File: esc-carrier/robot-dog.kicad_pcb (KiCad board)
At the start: 2 copper layers, 74.3 x 78.1 mm, 35 parts, among them J1 Conn_01x02, J10 Conn_01x02, J11 Conn_01x04, J12 Conn_01x04, J13 Conn_01x04, J2 Conn_01x04, J3 Conn_01x04, J4 Conn_01x03, J5 Conn_01x05, J6 Conn_01x05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

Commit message: Final version for manufacture
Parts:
- added REF**: MountingHole_3.2mm_M3_Pad, MountingHole:MountingHole_3.2mm_M3_Pad, F.Cu at (196.5, 94.2)
- added REF**: MountingHole_3.2mm_M3_Pad, MountingHole:MountingHole_3.2mm_M3_Pad, F.Cu at (210.7, 40.9)
- added REF**: MountingHole_3.2mm_M3_Pad, MountingHole:MountingHole_3.2mm_M3_Pad, F.Cu at (146.1, 40.9)
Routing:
- net Net-(J11-Pad1): track 137.1 -> 139.0 mm
- net Net-(J11-Pad2): track 128.5 -> 129.2 mm
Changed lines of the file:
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@@
       (outputformat 1)
       (mirror false)
-      (drillshape 1)
+      (drillshape 0)
       (scaleselection 1)
-      (outputdirectory "")
+      (outputdirectory "out")
     )
   )
@@
     )
   )
+  (footprint "MountingHole:MountingHole_3.2mm_M3_Pad" (layer "F.Cu")
+    (at 196.469 94.234)
+    (descr "Mounting Hole 3.2mm, M3")
+    (tags "mounting hole 3.2mm m3")
+    (attr exclude_from_pos_files exclude_from_bom)
+    (fp_text reference "REF**" (at 0 -4.2) (layer "F.SilkS") hide
+      (effects (font (size 1 1) (thickness 0.15)))
+    )
+    (fp_text value "MountingHole_3.2mm_M3_Pad" (at 0 4.2) (layer "F.Fab")
+      (effects (font (size 1 1) (thickness 0.15)))
+    )
+    (fp_text user "${REFERENCE}" (at 0 0) (layer "F.Fab")
+      (effects (font (size 1 1) (thickness 0.15)))
+    )
+    (fp_circle (center 0 0) (end 3.2 0) (layer "Cmts.User") (width 0.15) (fill none))
+    (fp_circle (center 0 0) (end 3.45 0) (layer "F.CrtYd") (width 0.05) (fill none))
+    (pad "1" thru_hole circle (at 0 0) (size 6.4 6.4) (drill 3.2) (layers F&B.Cu *.Mask))
+  )
   (footprint "Connector_PinHeader_2.54mm:PinHeader_1x04_P2.54mm_Vertical" (layer "F.Cu")
     (at 211.582 67.564)
@@
     )
   )
+  (footprint "MountingHole:MountingHole_3.2mm_M3_Pad" (layer "F.Cu")
+    (at 210.693 40.894)
+    (descr "Mounting Hole 3.2mm, M3")
+    (tags "mounting hole 3.2mm m3")
+    (attr exclude_from_pos_files exclude_from_bom)
+    (fp_text reference "REF**" (at 0 -4.2) (layer "F.SilkS") hide
+      (effects (font (size 1 1) (thickness 0.15)))
+    )
+    (fp_text value "MountingHole_3.2mm_M3_Pad" (at 0 4.2) (layer "F.Fab")
+      (effects (font (size 1 1) (thickness 0.15)))
+    )
+    (fp_text user "${REFERENCE}" (at 0 0) (layer "F.Fab")
+      (effects (font (size 1 1) (thickness 0.15)))
+    )
+    (fp_circle (center 0 0) (end 3.2 0) (layer "Cmts.User") (width 0.15) (fill none))
+    (fp_circle (center 0 0) (end 3.45 0) (layer "F.CrtYd") (width 0.05) (fill none))
+    (pad "1" thru_hole circle (at 0 0) (size 6.4 6.4) (drill 3.2) (layers F&B.Cu *.Mask))
+  )
   (footprint "LED_SMD:LED_0603_1608Metric_Pad1.05x0.95mm_HandSolder" (layer "F.Cu")
     (at 209.931 101.473)
@@
     )
   )
+  (footprint "MountingHole:MountingHole_3.2mm_M3_Pad" (layer "F.Cu")
+    (at 146.05 40.894)
+    (descr "Mounting Hole 3.2mm, M3")
+    (tags "mounting hole 3.2mm m3")
+    (attr exclude_from_pos_files exclude_from_bom)
+    (fp_text reference "REF**" (at 0 -4.2) (layer "F.SilkS") hide
+      (effects (font (size 1 1) (thickness 0.15)))
+    )
+    (fp_text value "MountingHole_3.2mm_M3_Pad" (at 0 4.2) (layer "F.Fab")
+      (effects (font (size 1 1) (thickness 0.15)))
+    )
+    (fp_text user "${REFERENCE}" (at 0 0) (layer "F.Fab")
+      (effects (font (size 1 1) (thickness 0.15)))
+    )
+    (fp_circle (center 0 0) (end 3.2 0) (layer "Cmts.User") (width 0.15) (fill none))
+    (fp_circle (center 0 0) (end 3.45 0) (layer "F.CrtYd") (width 0.05) (fill none))
+    (pad "1" thru_hole circle (at 0 0) (size 6.4 6.4) (drill 3.2) (layers *.Cu *.Mask))
+  )
   (footprint "DogESCCarrier:ESC-I2C-Pads" (layer "F.Cu")
     (at 168.148 79.12)
@@
     (effects (font (size 1.2 1.2) (thickness 0.2) italic))
   )
-  (gr_text "VCC" (at 147.955 44.196) (layer "F.SilkS")
+  (gr_text "VCC" (at 148.209 45.974) (layer "F.SilkS")
     (effects (font (size 1.2 1.2) (thickness 0.2) italic))
   )
@@
   (segment (start 168.148 79.12) (end 168.148 84.1775) (width 1) (layer "F.Cu") (net 12))
   (segment (start 178.816 59.309) (end 180.466 60.959) (width 0.25) (layer "F.Cu") (net 13))
+  (segment (start 178.817 79.121) (end 178.817 81.154) (width 0.25) (layer "F.Cu") (net 13))
   (segment (start 180.466 60.959) (end 201.93 60.959) (width 0.25) (layer "F.Cu") (net 13))
+  (segment (start 178.817 102.998) (end 180.467 104.648) (width 0.25) (layer "F.Cu") (net 13))
   (segment (start 178.817 81.154) (end 180.467 82.804) (width 0.25) (layer "F.Cu") (net 13))
-  (segment (start 178.817 102.998) (end 180.467 104.648) (width 0.25) (layer "F.Cu") (net 13))
   (segment (start 180.467 104.648) (end 201.931 104.648) (width 0.25) (layer "F.Cu") (net 13))
   (segment (start 178.816 57.276) (end 178.816 59.309) (width 0.25) (layer "F.Cu") (net 13))
-  (segment (start 180.467 82.804) (end 201.931 82.804) (width 0.25) (layer "F.Cu") (net 13))
-  (segment (start 178.817 79.121) (end 178.817 81.154) (width 0.25) (layer "F.Cu") (net 13))
+  (segment (start 180.467 82.804) (end 202.702734 82.804) (width 0.25) (layer "F.Cu") (net 13))
+  (segment (start 202.702734 82.804) (end 202.7815 82.882766) (width 0.25) (layer "F.Cu") (net 13))
   (segment (start 178.817 100.965) (end 178.817 102.998) (width 0.25) (layer "F.Cu") (net 13))
   (via (at 201.929 104.648) (size 0.8) (drill 0.4) (layers "F.Cu" "B.Cu") (net 13))
-  (via (at 201.93 82.804) (size 0.8) (drill 0.4) (layers "F.Cu" "B.Cu") (net 13))
+  (via (at 202.7815 82.882766) (size 0.8) (drill 0.4) (layers "F.Cu" "B.Cu") (net 13))
   (via (at 201.93 60.959) (size 0.8) (drill 0.4) (layers "F.Cu" "B.Cu") (net 13))
+  (segment (start 201.93 82.031266) (end 202.7815 82.882766) (width 0.25) (layer "B.Cu") (net 13))
+  (segment (start 201.93 60.959) (end 201.93 82.031266) (width 0.25) (layer "B.Cu") (net 13))
   (segment (start 201.93 48.768) (end 201.93 60.959) (width 0.25) (layer "B.Cu") (net 13))
-  (segment (start 201.93 82.804) (end 201.93 104.647) (width 0.25) (layer "B.Cu") (net 13))
-  (segment (start 201.93 60.959) (end 201.93 82.804) (width 0.25) (layer "B.Cu") (net 13))
+  (segment (start 203.073 83.174266) (end 202.7815 82.882766) (width 0.25) (layer "B.Cu") (net 13))
+  (segment (start 203.073 103.504) (end 203.073 83.174266) (width 0.25) (layer "B.Cu") (net 13))
+  (segment (start 201.929 104.648) (end 203.073 103.504) (width 0.25) (layer "B.Cu") (net 13))
   (segment (start 199.263 46.101) (end 201.93 48.768) (width 0.25) (layer "B.Cu") (net 13))
-  (segment (start 201.93 104.647) (end 201.929 104.648) (width 0.25) (layer "B.Cu") (net 13))
   (segment (start 195.708 102.49) (end 195.708 101.854) (width 0.25) (layer "F.Cu") (net 14))
   (segment (start 194.566 103.632) (end 195.708 102.49) (width 0.25) (layer "F.Cu") (net 14))
@@
   (via (at 201.167 103.76) (size 0.8) (drill 0.4) (layers "F.Cu" "B.Cu") (net 16))
   (via (at 201.168 60.071) (size 0.8) (drill 0.4) (layers "F.Cu" "B.Cu") (net 16))
-  (segment (start 201.168 81.916) (end 201.168 103.759) (width 0.25) (layer "B.Cu") (net 16))
+  (segment (start 202.057 102.87) (end 201.167 103.76) (width 0.25) (layer "B.Cu") (net 16))
   (segment (start 196.723 46.101) (end 201.168 50.546) (width 0.25) (layer "B.Cu") (net 16))
-  (segment (start 201.168 103.759) (end 201.167 103.76) (width 0.25) (layer "B.Cu") (net 16))
   (segment (start 201.168 60.071) (end 201.168 81.916) (width 0.25) (layer "B.Cu") (net 16))
+  (segment (start 201.168 81.916) (end 202.057 82.805) (width 0.25) (layer "B.Cu") (net 16))
   (segment (start 201.168 50.546) (end 201.168 60.071) (width 0.25) (layer "B.Cu") (net 16))
+  (segment (start 202.057 82.805) (end 202.057 102.87) (width 0.25) (layer "B.Cu") (net 16))
   (segment (start 183.4505 59.943) (end 194.565 59.943) (width 0.25) (layer "F.Cu") (net 17))
   (segment (start 194.565 59.943) (end 195.707 58.801) (width 0.25) (layer "F.Cu") (net 17))

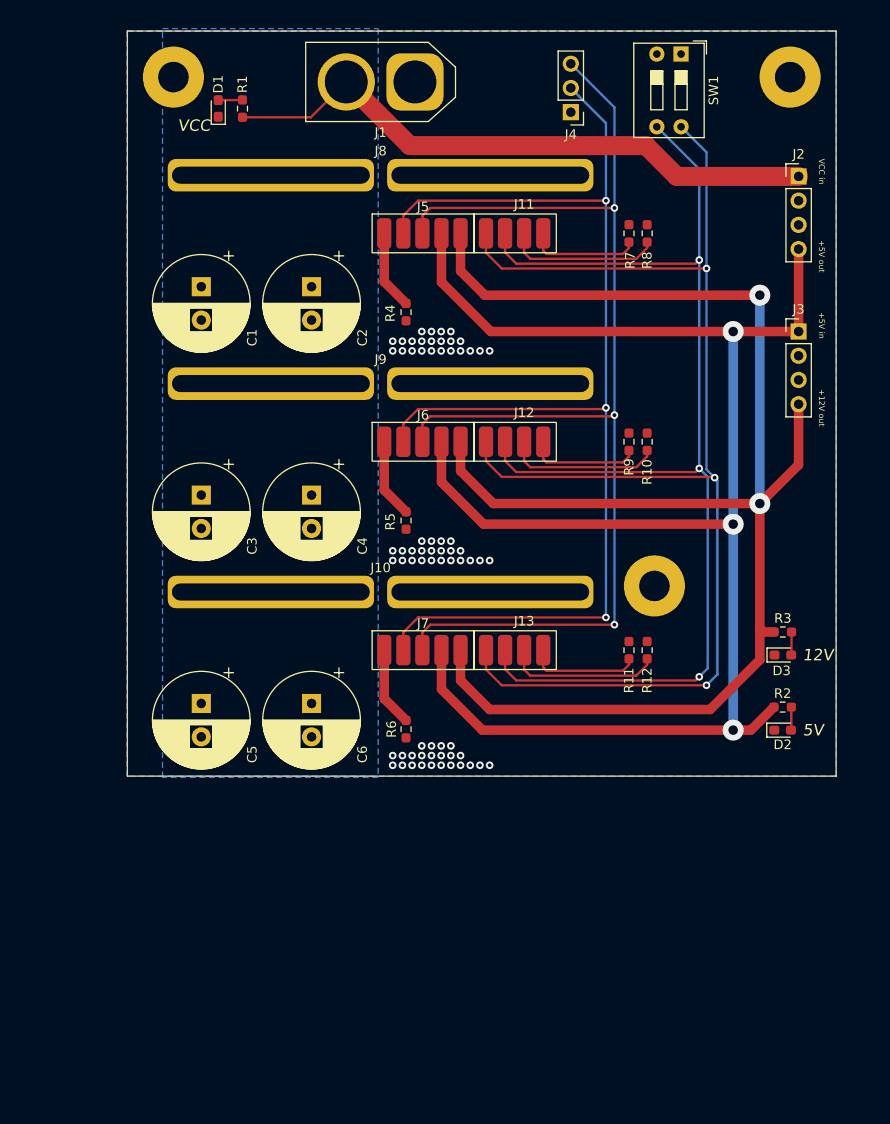
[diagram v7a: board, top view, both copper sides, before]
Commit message: fix power tab orientation
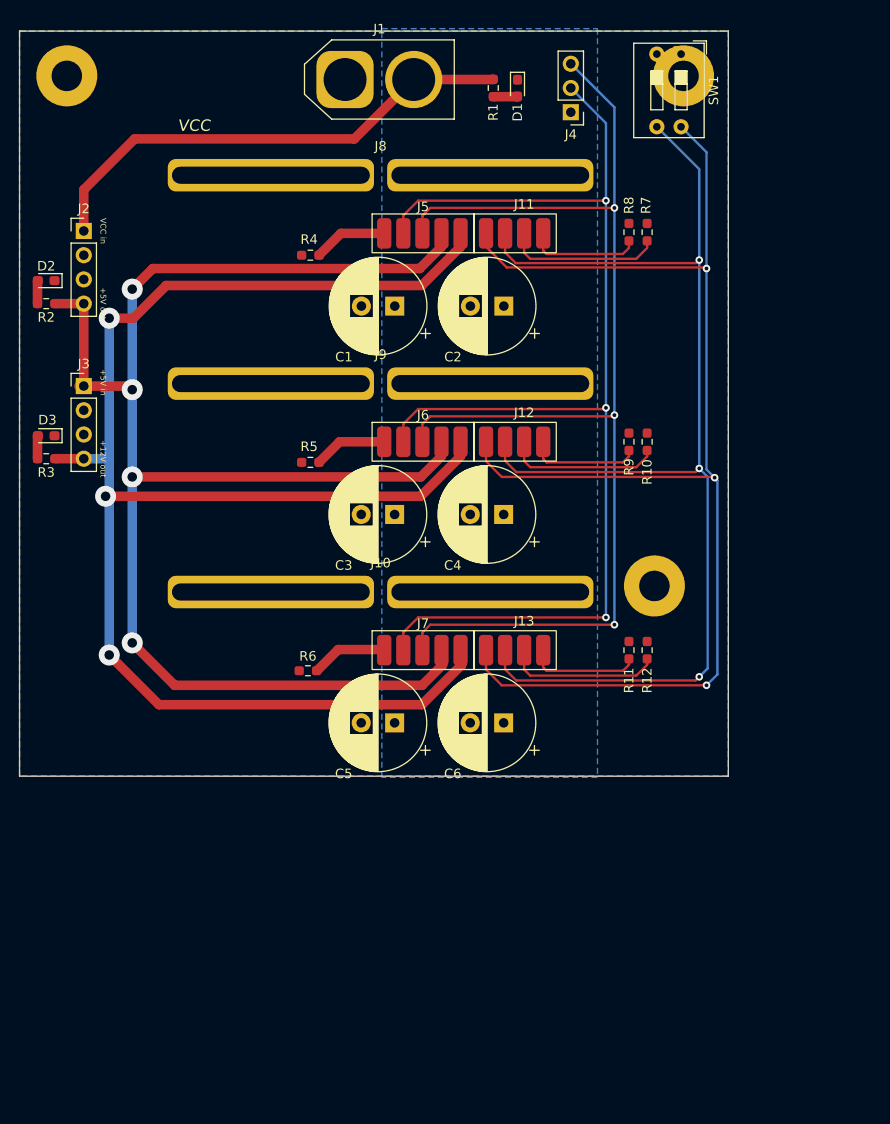
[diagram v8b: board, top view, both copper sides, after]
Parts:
- moved D2 90.4 mm to (132.7, 62.2), turned to 180 degrees
- moved R2 88.0 mm to (132.7, 64.6), turned to 180 degrees
- moved D3 80.6 mm to (132.7, 78.5), turned to 180 degrees
- moved R3 79.3 mm to (132.7, 80.9), turned to 180 degrees
- moved J2 75.1 mm to (136.7, 57.0)
- moved J3 75.1 mm to (136.7, 73.3)
- moved D1 31.4 mm to (182.1, 42.1), turned to -90 degrees
- moved R1 26.4 mm to (179.6, 42.0), turned to -90 degrees
- moved C1 20.4 mm to (169.3, 64.9), turned to 180 degrees
- moved C3 20.4 mm to (169.2, 86.7), turned to 180 degrees
- moved C5 20.4 mm to (169.2, 108.6), turned to 180 degrees
- moved C2 20.3 mm to (180.7, 64.9), turned to 180 degrees
- moved C4 20.2 mm to (180.7, 86.7), turned to 180 degrees
- moved C6 20.2 mm to (180.7, 108.6), turned to 180 degrees
- moved R6 12.0 mm to (160.1, 103.1), turned to 180 degrees
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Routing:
- net +5V: track 173.5 -> 161.5 mm, vias 3 -> 4
- net VCC: track 63.9 -> 52.0 mm
- net +12V: track 162.1 -> 164.9 mm, vias 2 -> 3
- net Net-(J7-Pad1): track 8.31 -> 7.73 mm
- net Net-(J6-Pad1): track 8.29 -> 7.73 mm
- net Net-(J5-Pad1): track 8.29 -> 7.78 mm
- net GND: vias 69 -> 0
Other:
- board text removed: "12V"
- board text removed: "5V"
